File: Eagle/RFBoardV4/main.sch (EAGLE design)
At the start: 28 parts, among them Q1 8/16/20MHz, U1 ATMEGA328

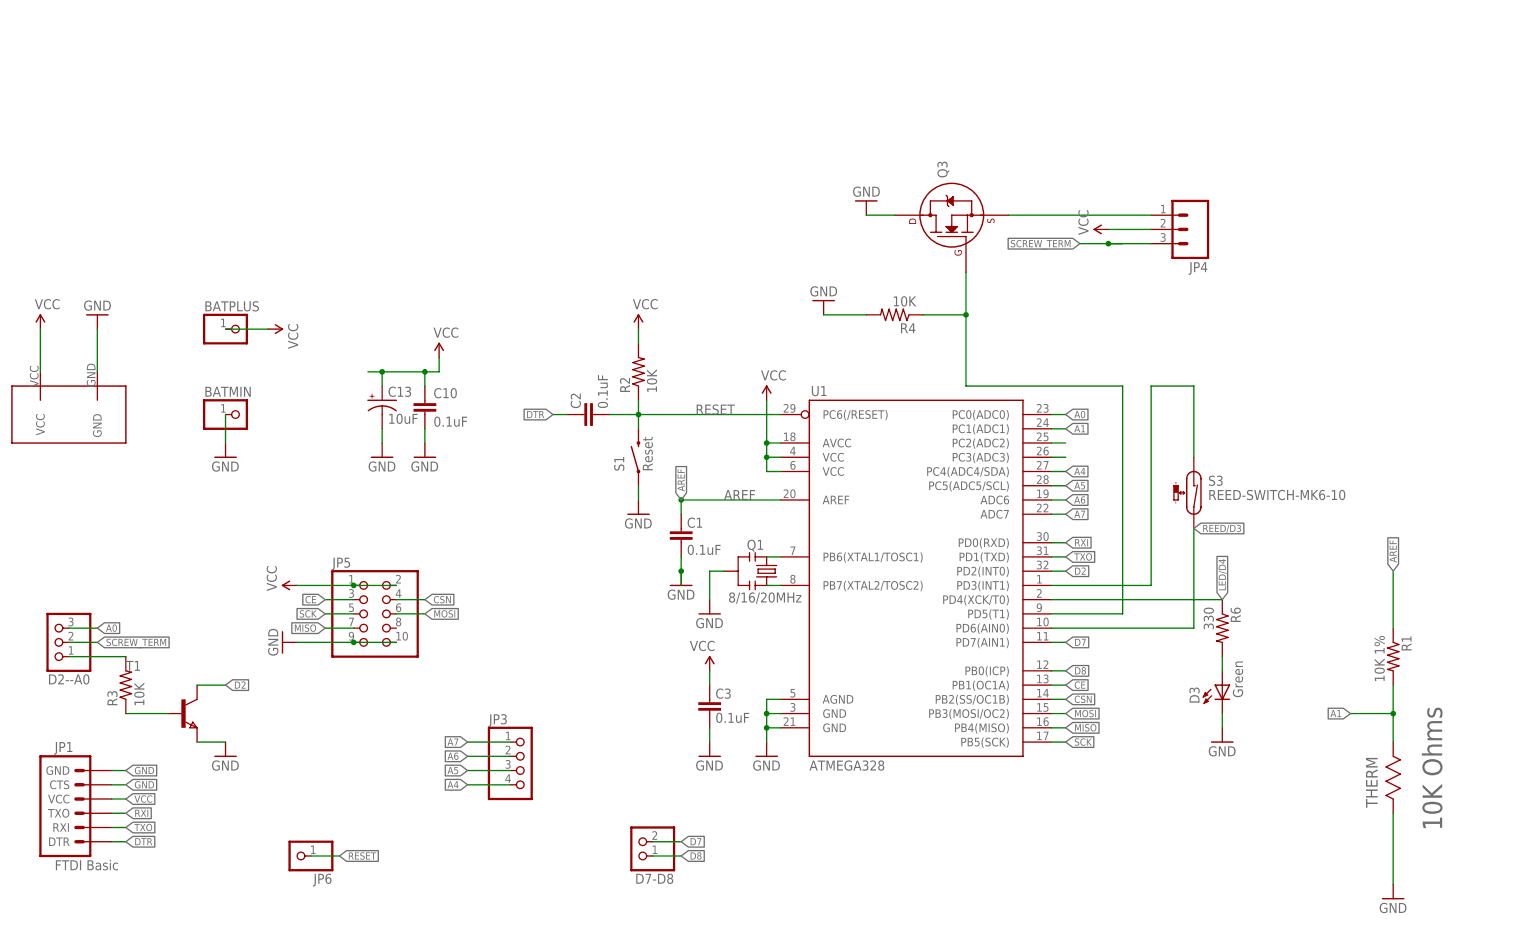
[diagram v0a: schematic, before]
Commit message: 4.x support + 4.1 pcb layout + cleanup
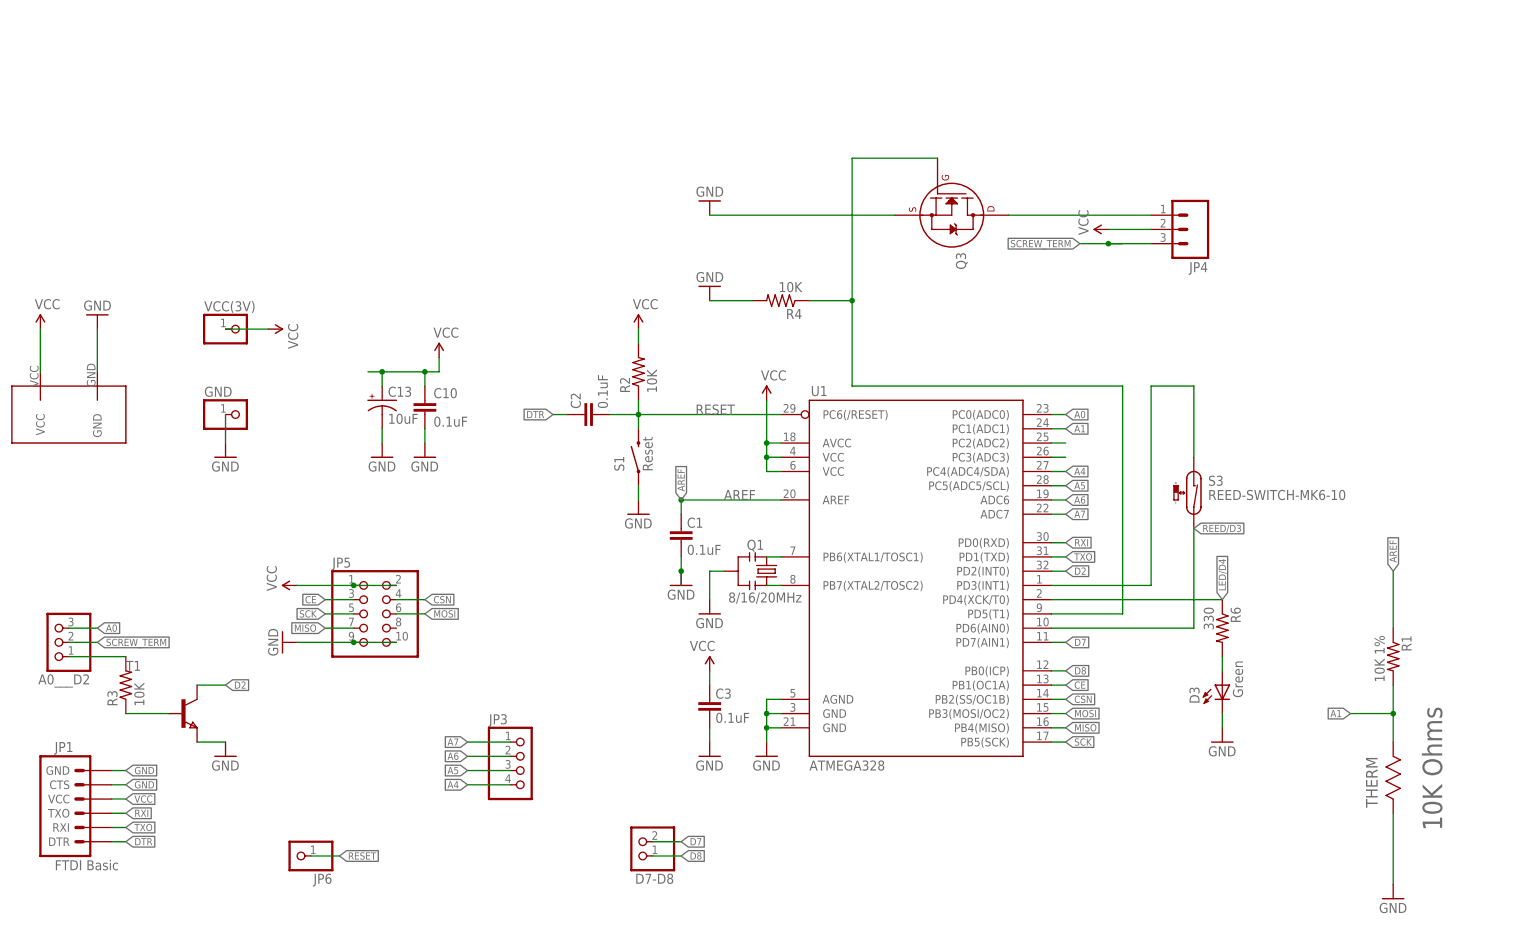
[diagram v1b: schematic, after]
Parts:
- renumbered BATMIN to GND, BATPLUS to VCC(3V), D2--A0 to A0___D2
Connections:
- removed net SCREW_GND: JP4.1, Q3.S
- new net N$4: JP4.1, Q3.D
- net GND: now also Q3.S; no longer Q3.D
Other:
- moved on the sheet: Q3, R4
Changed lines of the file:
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@@
 <?xml version="1.0" encoding="utf-8"?>
 <!DOCTYPE eagle SYSTEM "eagle.dtd">
-<eagle version="7.1.0">
+<eagle version="7.2.0">
 <drawing>
 <settings>
@@
 <part name="S1" library="Testing" deviceset="SWITCH-MOMENTARY-2" device="SMD-ALT01" value="Reset"/>
 <part name="Q1" library="Testing" deviceset="RESONATOR" device="1:1" value="8/16/20MHz"/>
-<part name="BATPLUS" library="pinhead" deviceset="PINHD-1X1" device=""/>
-<part name="BATMIN" library="pinhead" deviceset="PINHD-1X1" device=""/>
+<part name="VCC(3V)" library="pinhead" deviceset="PINHD-1X1" device=""/>
+<part name="GND" library="pinhead" deviceset="PINHD-1X1" device=""/>
 <part name="P+2" library="SparkFun" deviceset="3.3V" device="" value="VCC"/>
 <part name="GND13" library="SparkFun" deviceset="GND" device=""/>
@@
 <part name="R1" library="SparkFun" deviceset="RESISTOR" device="0603-RES" value="10K 1%"/>
 <part name="THERM" library="Vishay_By_element14_Batch_1" deviceset="NTCS0603E3103HMT" device="" value="10K Ohms"/>
-<part name="D2--A0" library="pinhead" deviceset="PINHD-1X3" device=""/>
+<part name="A0___D2" library="pinhead" deviceset="PINHD-1X3" device=""/>
 <part name="GND2" library="SparkFun" deviceset="GND" device=""/>
 <part name="JP5" library="pinhead" deviceset="PINHD-2X5" device=""/>
@@
 <attribute name="VALUE" x="137.922" y="121.412" size="1.778" layer="96"/>
 </instance>
-<instance part="BATPLUS" gate="G$1" x="50.8" y="170.18"/>
-<instance part="BATMIN" gate="G$1" x="50.8" y="154.94"/>
+<instance part="VCC(3V)" gate="G$1" x="50.8" y="170.18"/>
+<instance part="GND" gate="G$1" x="50.8" y="154.94"/>
 <instance part="P+2" gate="G$1" x="55.88" y="170.18" rot="R270"/>
 <instance part="GND13" gate="1" x="48.26" y="147.32"/>
@@
 <instance part="R1" gate="G$1" x="256.54" y="111.76" rot="R270"/>
 <instance part="THERM" gate="A" x="256.54" y="83.82" rot="R90"/>
-<instance part="D2--A0" gate="A" x="17.78" y="114.3" rot="R180"/>
+<instance part="A0___D2" gate="A" x="17.78" y="114.3" rot="R180"/>
 <instance part="GND2" gate="1" x="256.54" y="68.58"/>
 <instance part="JP5" gate="A" x="73.66" y="119.38"/>
@@
 <instance part="JP4" gate="G$1" x="220.98" y="187.96" rot="R180"/>
 <instance part="P+5" gate="G$1" x="205.74" y="187.96" rot="R90"/>
-<instance part="GND10" gate="1" x="162.56" y="193.04" rot="R180"/>
-<instance part="R4" gate="G$1" x="167.64" y="172.72" rot="R180"/>
-<instance part="GND11" gate="1" x="154.94" y="175.26" rot="R180"/>
-<instance part="Q3" gate="G$1" x="177.8" y="190.5" rot="R90"/>
+<instance part="GND10" gate="1" x="134.62" y="193.04" rot="R180"/>
+<instance part="R4" gate="G$1" x="147.32" y="175.26" rot="R180"/>
+<instance part="GND11" gate="1" x="134.62" y="177.8" rot="R180"/>
+<instance part="Q3" gate="G$1" x="177.8" y="190.5" rot="R270"/>
 <instance part="U$1" gate="G$1" x="43.18" y="147.32"/>
 <instance part="P+6" gate="G$1" x="15.24" y="170.18"/>
@@
 </segment>
 <segment>
-<pinref part="BATMIN" gate="G$1" pin="1"/>
+<pinref part="GND" gate="G$1" pin="1"/>
 <pinref part="GND13" gate="1" pin="GND"/>
 <wire x1="48.26" y1="154.94" x2="48.26" y2="149.86" width="0.1524" layer="91"/>
@@
 <pinref part="R4" gate="G$1" pin="2"/>
 <pinref part="GND11" gate="1" pin="GND"/>
-<wire x1="162.56" y1="172.72" x2="154.94" y2="172.72" width="0.1524" layer="91"/>
-</segment>
-<segment>
-<pinref part="Q3" gate="G$1" pin="D"/>
-<pinref part="GND10" gate="1" pin="GND"/>
-<wire x1="167.64" y1="190.5" x2="162.56" y2="190.5" width="0.1524" layer="91"/>
+<wire x1="142.24" y1="175.26" x2="134.62" y2="175.26" width="0.1524" layer="91"/>
 </segment>
 <segment>
@@
 <pinref part="U$1" gate="G$1" pin="GND"/>
 <wire x1="25.4" y1="170.18" x2="25.4" y2="162.56" width="0.1524" layer="91"/>
+</segment>
+<segment>
+<pinref part="Q3" gate="G$1" pin="S"/>
+<pinref part="GND10" gate="1" pin="GND"/>
+<wire x1="167.64" y1="190.5" x2="134.62" y2="190.5" width="0.1524" layer="91"/>
 </segment>
 </net>
@@
 </segment>
 <segment>
-<pinref part="BATPLUS" gate="G$1" pin="1"/>
+<pinref part="VCC(3V)" gate="G$1" pin="1"/>
 <pinref part="P+2" gate="G$1" pin="3.3V"/>
 <wire x1="48.26" y1="170.18" x2="55.88" y2="170.18" width="0.1524" layer="91"/>
@@
 </segment>
 <segment>
-<pinref part="D2--A0" gate="A" pin="3"/>
+<pinref part="A0___D2" gate="A" pin="3"/>
 <wire x1="20.32" y1="116.84" x2="25.4" y2="116.84" width="0.1524" layer="91"/>
 <label x="25.4" y="116.84" size="1.27" layer="95" xref="yes"/>
@@
 <net name="SCREW_TERM" class="0">
 <segment>
-<pinref part="D2--A0" gate="A" pin="2"/>
+<pinref part="A0___D2" gate="A" pin="2"/>
 <wire x1="20.32" y1="114.3" x2="25.4" y2="114.3" width="0.1524" layer="91"/>
 <label x="25.4" y="114.3" size="1.27" layer="95" xref="yes"/>
@@
 <pinref part="U1" gate="G$1" pin="PD5(T1)"/>
 <wire x1="195.58" y1="119.38" x2="208.28" y2="119.38" width="0.1524" layer="91"/>
-<wire x1="180.34" y1="172.72" x2="180.34" y2="160.02" width="0.1524" layer="91"/>
-<wire x1="180.34" y1="160.02" x2="208.28" y2="160.02" width="0.1524" layer="91"/>
+<wire x1="160.02" y1="175.26" x2="160.02" y2="160.02" width="0.1524" layer="91"/>
+<wire x1="160.02" y1="160.02" x2="208.28" y2="160.02" width="0.1524" layer="91"/>
 <wire x1="208.28" y1="160.02" x2="208.28" y2="119.38" width="0.1524" layer="91"/>
 <pinref part="R4" gate="G$1" pin="1"/>
-<wire x1="172.72" y1="172.72" x2="180.34" y2="172.72" width="0.1524" layer="91"/>
+<wire x1="152.4" y1="175.26" x2="160.02" y2="175.26" width="0.1524" layer="91"/>
 <pinref part="Q3" gate="G$1" pin="G"/>
-<wire x1="180.34" y1="180.34" x2="180.34" y2="172.72" width="0.1524" layer="91"/>
-<junction x="180.34" y="172.72"/>
+<junction x="160.02" y="175.26"/>
+<wire x1="160.02" y1="175.26" x2="160.02" y2="200.66" width="0.1524" layer="91"/>
+<wire x1="160.02" y1="200.66" x2="175.26" y2="200.66" width="0.1524" layer="91"/>
 </segment>
 </net>
 <net name="N$3" class="0">
 <segment>
-<pinref part="D2--A0" gate="A" pin="1"/>
+<pinref part="A0___D2" gate="A" pin="1"/>
 <wire x1="20.32" y1="111.76" x2="30.48" y2="111.76" width="0.1524" layer="91"/>
 <pinref part="R3" gate="G$1" pin="2"/>
@@
 </segment>
 </net>
-<net name="SCREW_GND" class="2">
+<net name="N$4" class="2">
 <segment>
 <pinref part="JP4" gate="G$1" pin="1"/>
-<pinref part="Q3" gate="G$1" pin="S"/>
+<pinref part="Q3" gate="G$1" pin="D"/>
 <wire x1="213.36" y1="190.5" x2="187.96" y2="190.5" width="0.1524" layer="91"/>
 </segment>

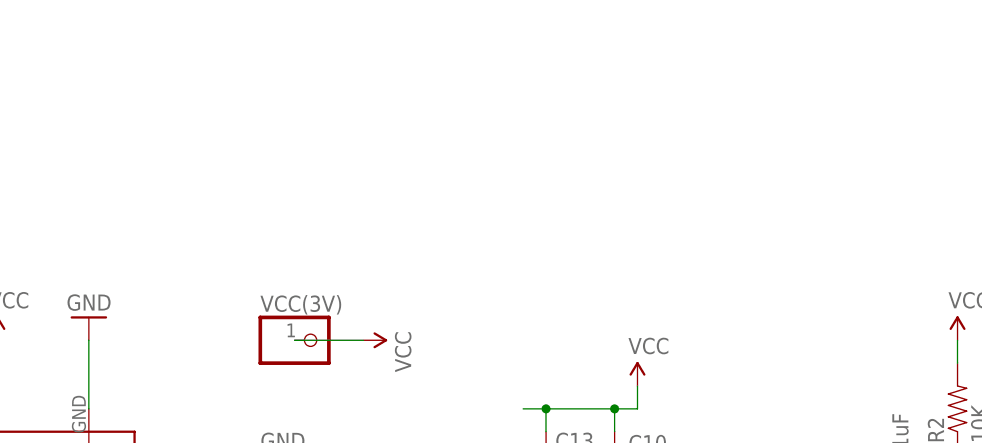
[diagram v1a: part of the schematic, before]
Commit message: Adding power boost - still WIP
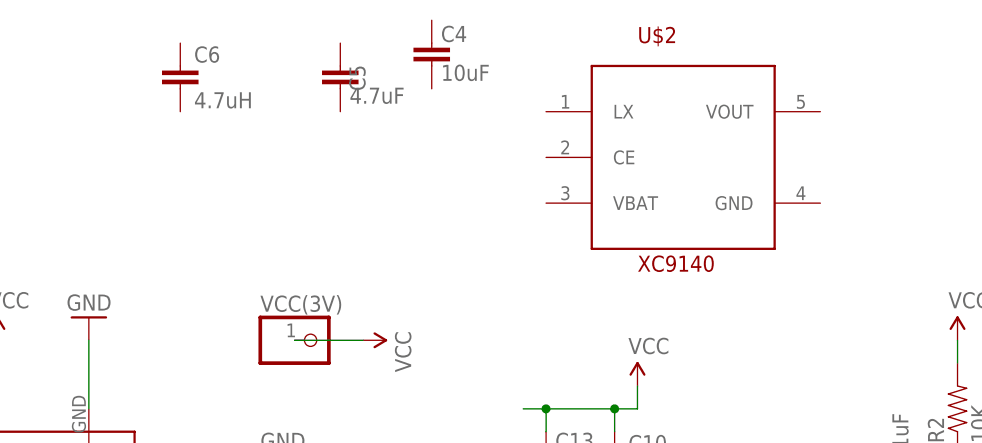
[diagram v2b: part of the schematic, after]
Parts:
- added C4: 10uF, SparkFun:CAP0603-CAP
- added C5: 4.7uF, SparkFun:CAP0603-CAP
- added C6: 4.7uH, SparkFun:CAP0805
- added U$2: XC9140, boost:XC9140
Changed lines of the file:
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@@
 <?xml version="1.0" encoding="utf-8"?>
 <!DOCTYPE eagle SYSTEM "eagle.dtd">
-<eagle version="7.2.0">
+<eagle version="7.5.0">
 <drawing>
 <settings>
@@
 <layer number="112" name="tSilk" color="7" fill="1" visible="yes" active="yes"/>
 <layer number="113" name="IDFDebug" color="4" fill="1" visible="yes" active="yes"/>
+<layer number="114" name="FRNTMAAT1" color="7" fill="1" visible="yes" active="yes"/>
+<layer number="115" name="FRNTMAAT2" color="7" fill="1" visible="yes" active="yes"/>
 <layer number="116" name="Patch_BOT" color="9" fill="4" visible="yes" active="yes"/>
+<layer number="117" name="BACKMAAT1" color="7" fill="1" visible="yes" active="yes"/>
+<layer number="118" name="Rect_Pads" color="7" fill="1" visible="no" active="no"/>
+<layer number="119" name="KAP_TEKEN" color="7" fill="1" visible="yes" active="yes"/>
+<layer number="120" name="KAP_MAAT1" color="7" fill="1" visible="yes" active="yes"/>
 <layer number="121" name="_tsilk" color="7" fill="1" visible="yes" active="yes"/>
 <layer number="122" name="_bsilk" color="7" fill="1" visible="yes" active="yes"/>
@@
 <layer number="127" name="_tValues" color="7" fill="1" visible="yes" active="yes"/>
 <layer number="128" name="_bValues" color="7" fill="1" visible="yes" active="yes"/>
+<layer number="130" name="SMDSTROOK" color="7" fill="1" visible="yes" active="yes"/>
 <layer number="131" name="tAdjust" color="7" fill="1" visible="yes" active="yes"/>
 <layer number="132" name="bAdjust" color="7" fill="1" visible="yes" active="yes"/>
@@
 <layer number="223" name="223bmp" color="24" fill="1" visible="no" active="no"/>
 <layer number="224" name="224bmp" color="25" fill="1" visible="no" active="no"/>
+<layer number="225" name="225bmp" color="7" fill="1" visible="no" active="yes"/>
+<layer number="226" name="226bmp" color="7" fill="1" visible="no" active="yes"/>
+<layer number="227" name="227bmp" color="7" fill="1" visible="no" active="yes"/>
+<layer number="228" name="228bmp" color="7" fill="1" visible="no" active="yes"/>
+<layer number="230" name="230bmp" color="7" fill="1" visible="no" active="yes"/>
+<layer number="231" name="Eagle3D_PG1" color="7" fill="1" visible="yes" active="yes"/>
+<layer number="232" name="Eagle3D_PG2" color="7" fill="1" visible="yes" active="yes"/>
+<layer number="233" name="Eagle3D_PG3" color="7" fill="1" visible="yes" active="yes"/>
 <layer number="248" name="Housing" color="7" fill="1" visible="yes" active="yes"/>
 <layer number="249" name="Edge" color="7" fill="1" visible="yes" active="yes"/>
@@
 <layer number="251" name="SMDround" color="12" fill="11" visible="no" active="no"/>
 <layer number="254" name="cooling" color="7" fill="1" visible="yes" active="yes"/>
+<layer number="255" name="Accent" color="7" fill="1" visible="yes" active="yes"/>
 </layers>
 <schematic>
@@
 <part name="P+6" library="SparkFun" deviceset="3.3V" device="" value="VCC"/>
 <part name="GND12" library="SparkFun" deviceset="GND" device=""/>
+<part name="U$2" library="boost" deviceset="XC9140" device=""/>
+<part name="C4" library="SparkFun" deviceset="CAP" device="0603-CAP" value="10uF"/>
+<part name="C5" library="SparkFun" deviceset="CAP" device="0603-CAP" value="4.7uF"/>
+<part name="C6" library="SparkFun" deviceset="CAP" device="0805" value="4.7uH"/>
 </parts>
 <sheets>
@@
 <instance part="P+6" gate="G$1" x="15.24" y="170.18"/>
 <instance part="GND12" gate="1" x="25.4" y="172.72" rot="R180"/>
+<instance part="U$2" gate="IC1" x="91.44" y="190.5"/>
+<instance part="C4" gate="G$1" x="63.5" y="203.2" smashed="yes" rot="R180">
+<attribute name="NAME" x="64.516" y="203.327" size="1.778" layer="95"/>
+<attribute name="VALUE" x="64.516" y="199.009" size="1.778" layer="96"/>
+</instance>
+<instance part="C5" gate="G$1" x="53.34" y="200.66" smashed="yes" rot="R180">
+<attribute name="NAME" x="54.356" y="200.787" size="1.778" layer="95" rot="R270"/>
+<attribute name="VALUE" x="54.356" y="196.469" size="1.778" layer="96"/>
+</instance>
+<instance part="C6" gate="G$1" x="35.56" y="198.12"/>
 </instances>
 <busses>
